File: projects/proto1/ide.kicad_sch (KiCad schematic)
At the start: 1 part, among them J7 IDC_PATA

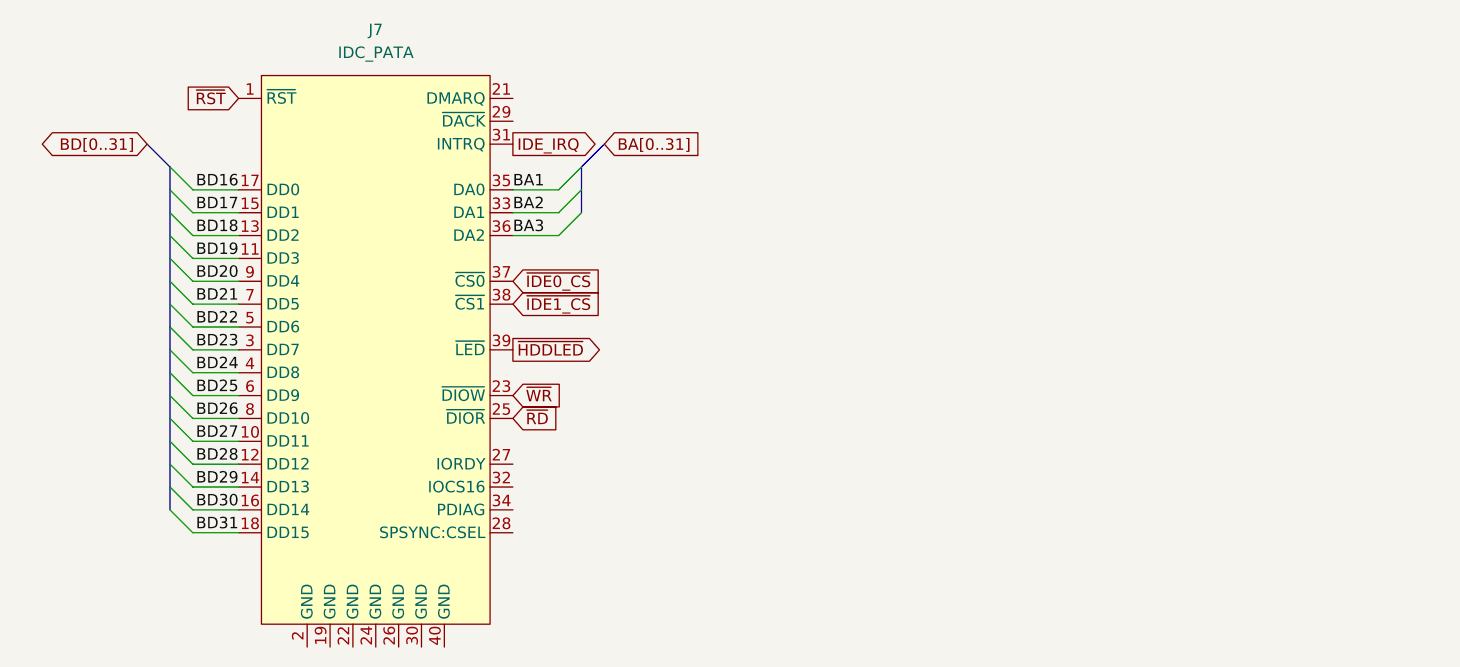
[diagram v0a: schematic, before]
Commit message: Renamed CMC to SCU, changed verification method to cocotb, and modified pcb schematic
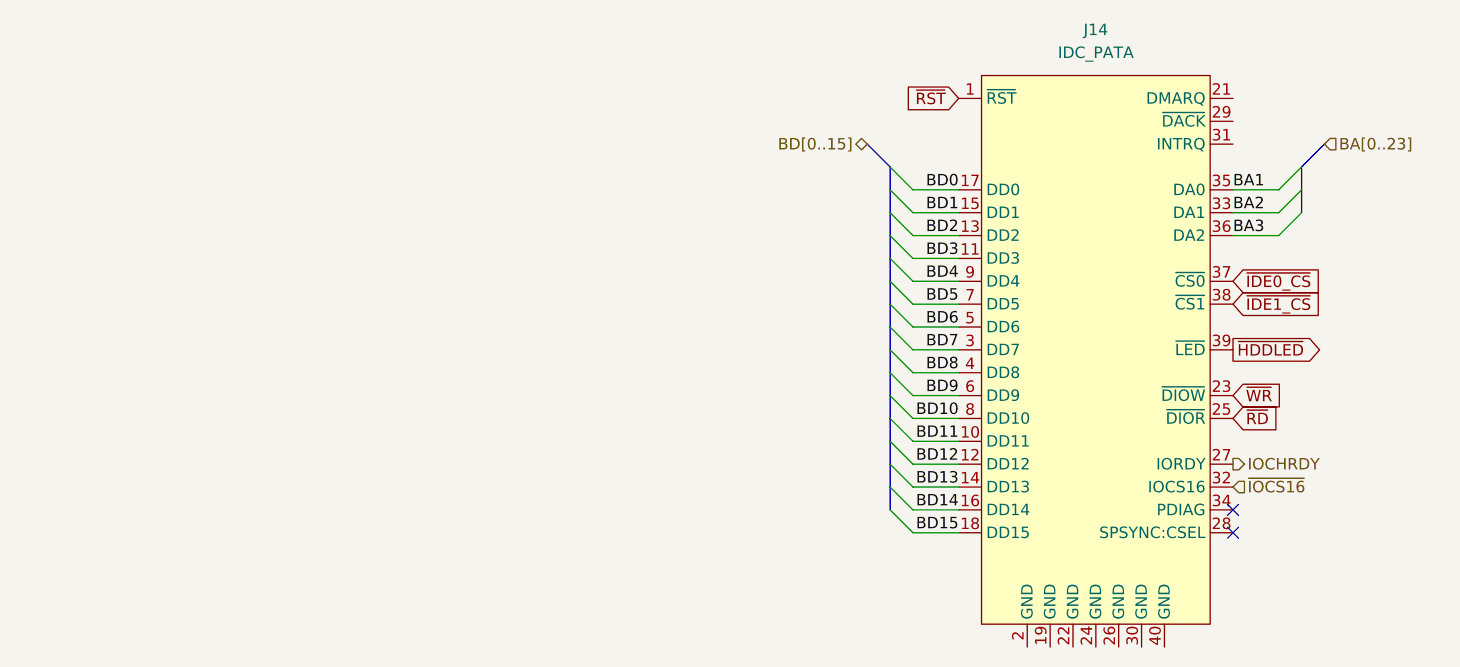
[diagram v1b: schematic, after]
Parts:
- renumbered J7 to J14
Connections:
- net IOCHRDY: now reaches J14.27 (IORDY)
- net ~{IOCS16}: now reaches J14.32 (IOCS16)
- net BD16 renamed BD0
- net BD17 renamed BD1
- net BD18 renamed BD2
- net BD19 renamed BD3
- net BD20 renamed BD4
- net BD21 renamed BD5
- net BD22 renamed BD6
- net BD23 renamed BD7
- net BD24 renamed BD8
- net BD25 renamed BD9
- net BD26 renamed BD10
- net BD27 renamed BD11
- net BD28 renamed BD12
- net BD29 renamed BD13
- net BD30 renamed BD14
- net BD31 renamed BD15
- net IDE_IRQ: no longer names the net of J14.31 (INTRQ)
- no-connect marks 0 -> 2
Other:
- moved on the sheet: J14
